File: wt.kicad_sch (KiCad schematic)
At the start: 20 parts, among them U1 STM32F407VGTx, Y1 Crystal_8Mhz

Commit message: working on AD inputs
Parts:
- removed C7: C-Pol-1uF-FK-V, Capacitor_SMD:C_1206_3216Metric, symbol eurorack:C-Pol-1uF-FK-V
- added C7: C-Pol-1uF-TAN, Capacitor_Tantalum_SMD:CP_EIA-3216-18_Kemet-A, symbol eurorack:C-Pol-1uF-TAN
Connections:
- net +3V3: now also C7.1
- net GND: now also C7.2

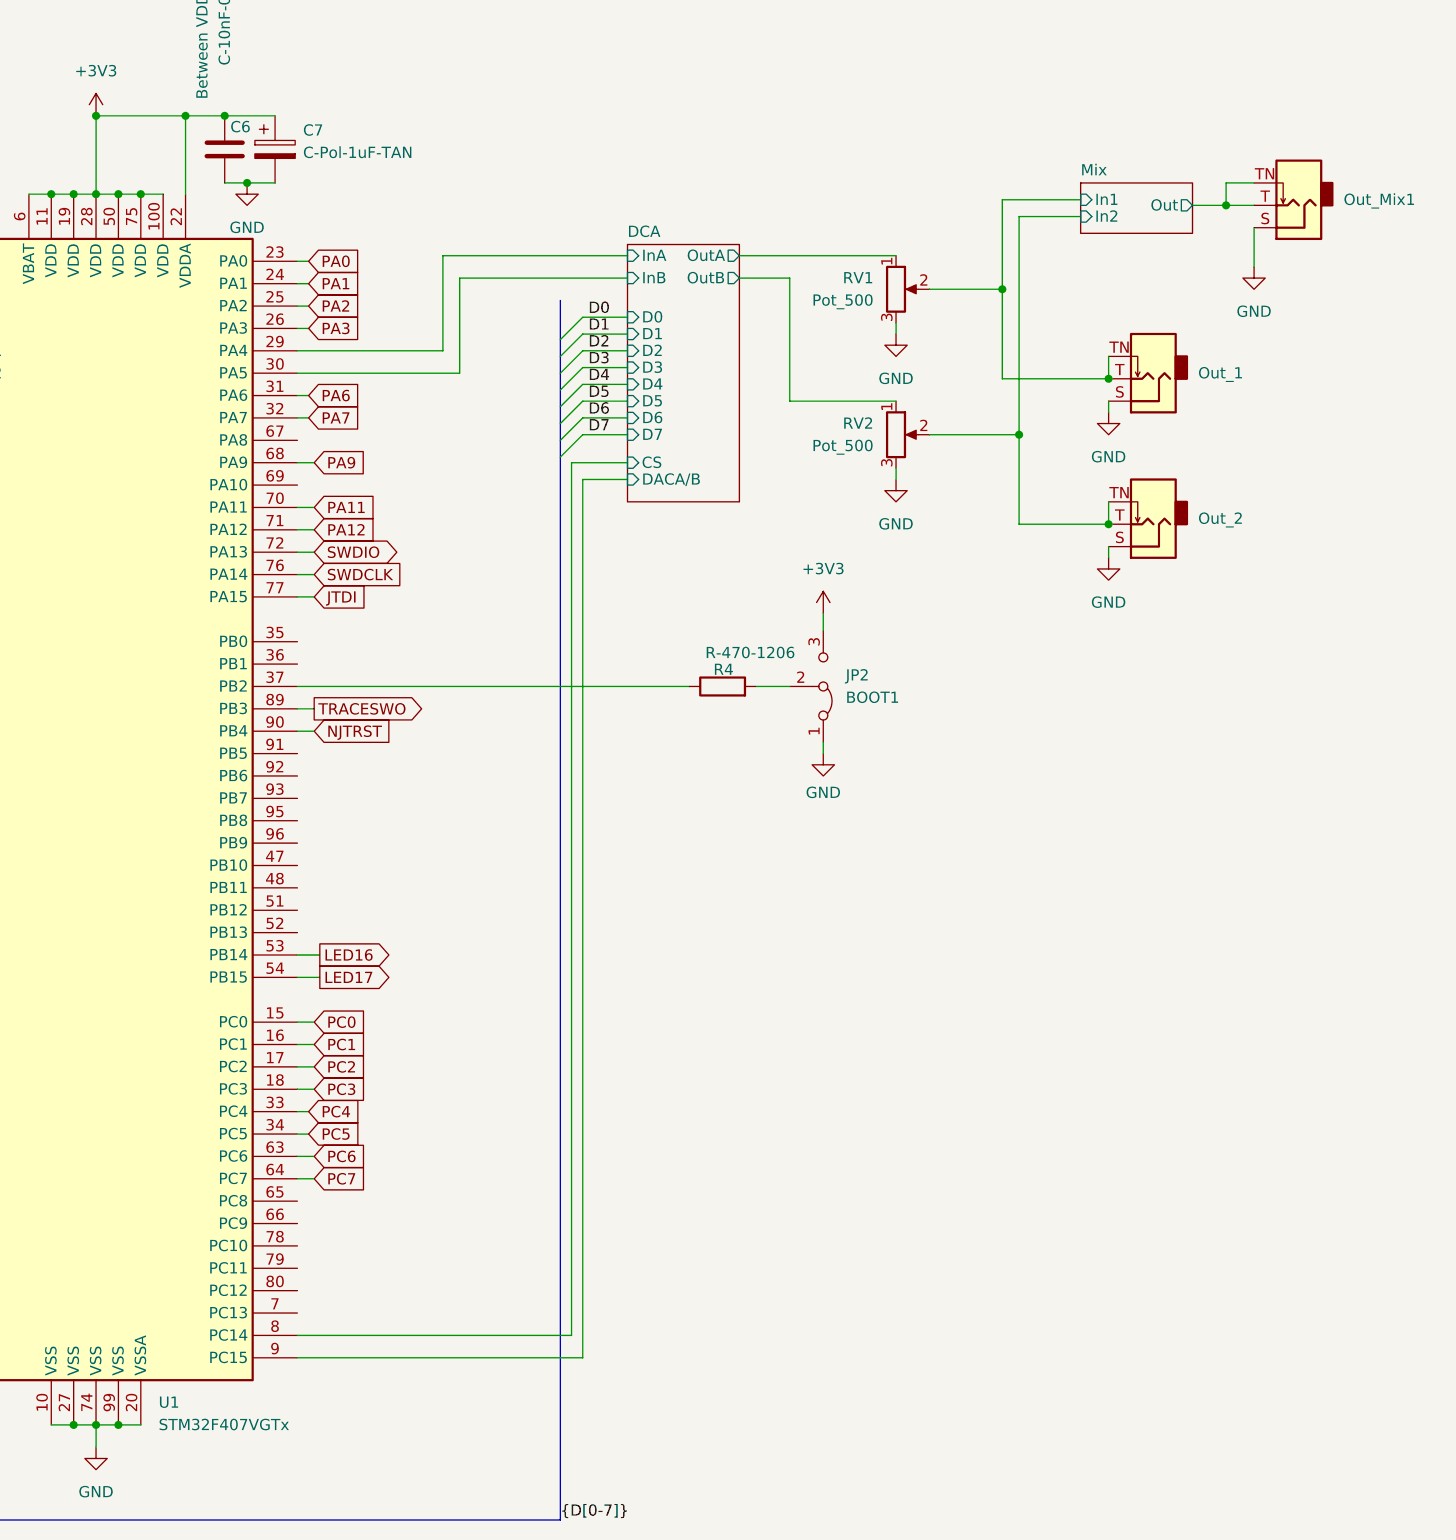
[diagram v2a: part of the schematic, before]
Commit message: reannotated changed to LM324
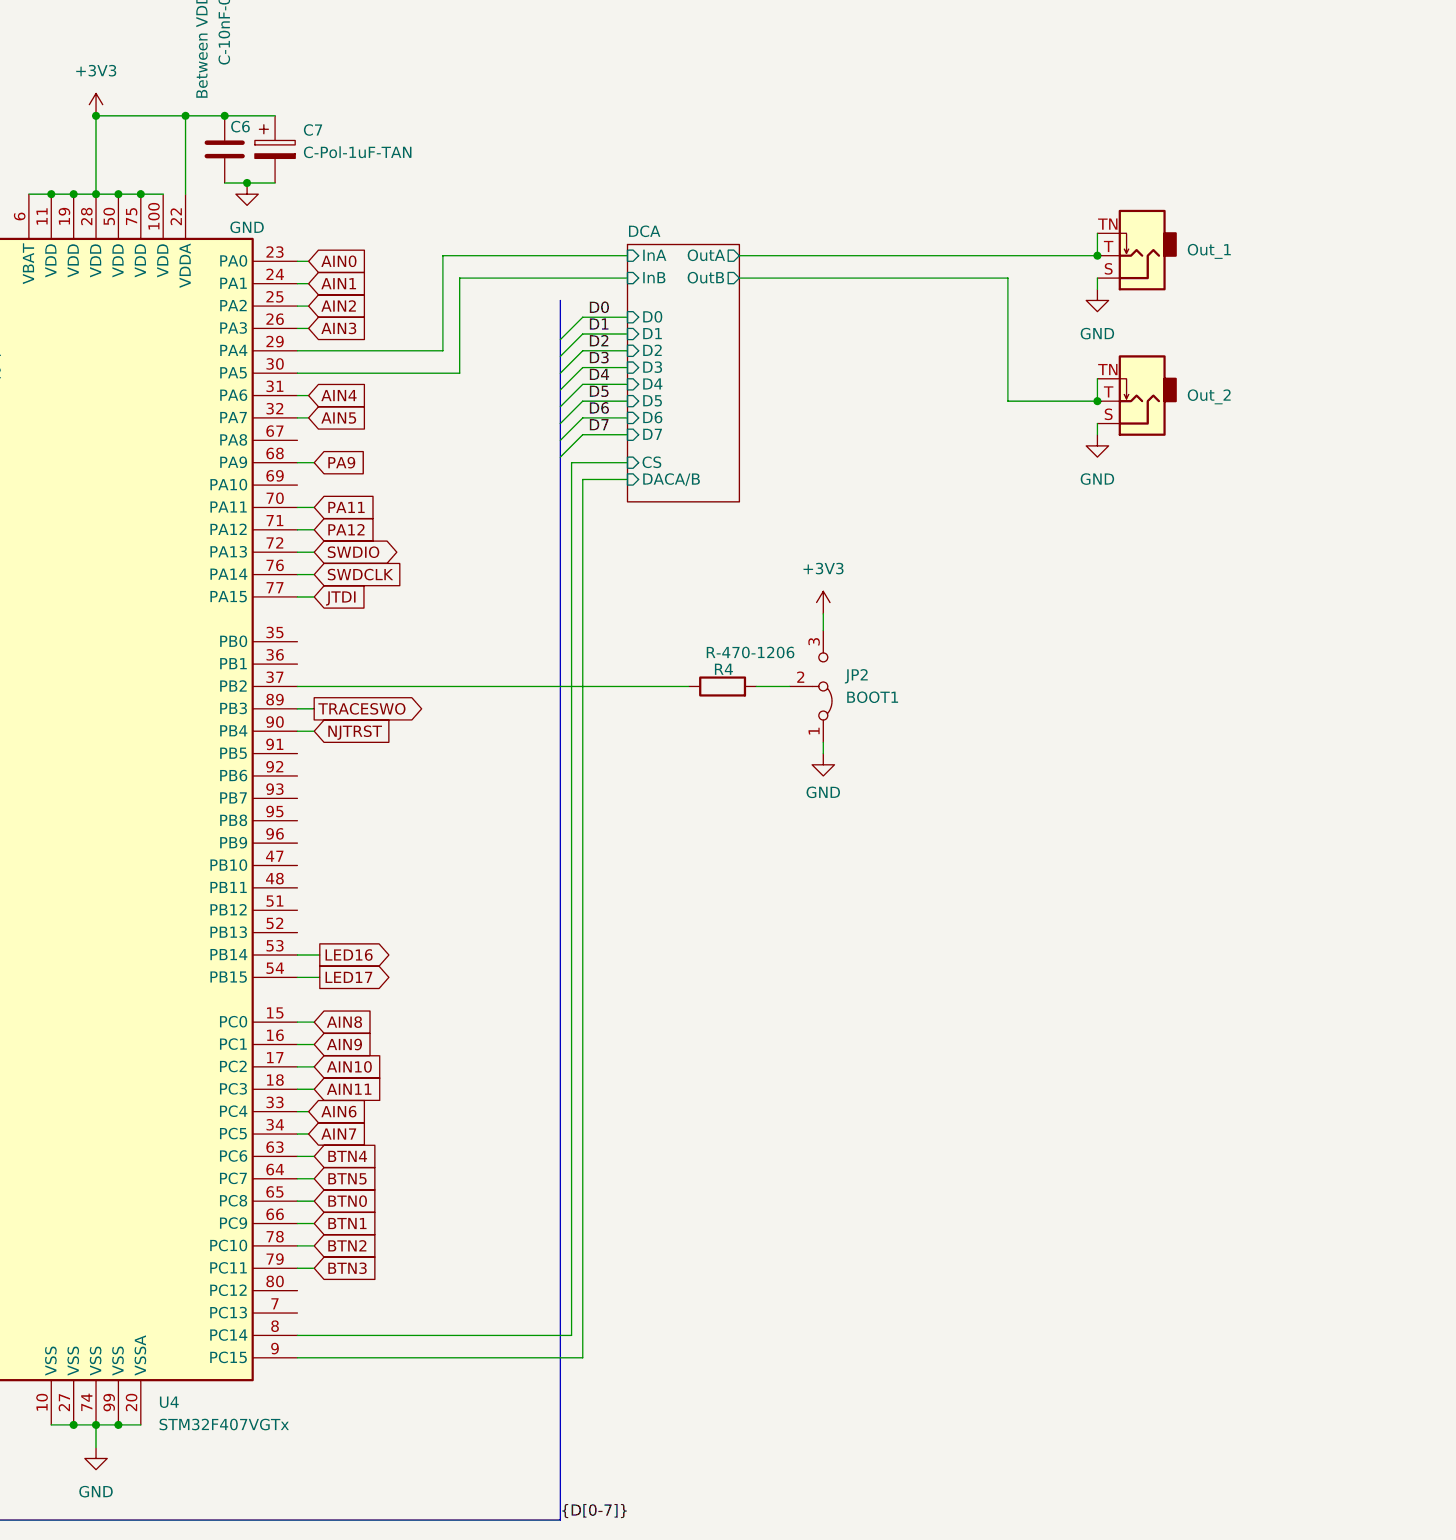
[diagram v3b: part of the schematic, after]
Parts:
- removed Out_Mix1: LUM-1502-03_3.5mm_mono_vertical_jack, eurorack:LUM 1502-03, symbol eurorack:LUM-1502-03_3.5mm_mono_vertical_jack
- removed RV1, RV2: Pot_500, Potentiometer_THT:Potentiometer_Piher_PT-10-V10_Vertical, symbol eurorack:Pot_500
- renumbered U1 to U4
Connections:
- net Mix/In1 is gone; now on net DCA/OutA: Out_1.T, Out_1.TN
- net Mix/In2 is gone; now on net DCA/OutB: Out_2.T, Out_2.TN
- net BTN0: now reaches U4.65 (PC8)
- net BTN1: now reaches U4.66 (PC9)
- net BTN2: now reaches U4.78 (PC10)
- net BTN3: now reaches U4.79 (PC11)
- net PA0 renamed AIN0
- net PA1 renamed AIN1
- net PA2 renamed AIN2
- net PA3 renamed AIN3
- net PA6 renamed AIN4
- net PA7 renamed AIN5
- net PC0 renamed AIN8
- net PC1 renamed AIN9
- net PC2 renamed AIN10
- net PC3 renamed AIN11
- net PC4 renamed AIN6
- net PC5 renamed AIN7
- net PC6 renamed BTN4
- net PC7 renamed BTN5
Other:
- removed sheet Mix
- moved on the sheet: Out_1, Out_2

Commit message: working on PCB, new iteratrion
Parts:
- JP1, JP2: footprint Connector_PinSocket_2.54mm:PinSocket_1x03_P2.54mm_Vertical -> Jumper:SolderJumper-3_P1.3mm_Open_RoundedPad1.0x1.5mm
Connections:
- net PA11 renamed USB_D-
- net PA12 renamed USB_D+
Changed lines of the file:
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@@
     )
   )
-  (global_label "PA12" (shape input) (at 210.82 125.73 0) (fields_autoplaced)
-    (effects (font (size 1.27 1.27)) (justify left))
-    (property "Intersheet References" "${INTERSHEET_REFS}" (id 0) (at 218.0107 125.6506 0)
+  (global_label "USB_D+" (shape input) (at 210.82 125.73 0) (fields_autoplaced)
+    (effects (font (size 1.27 1.27)) (justify left))
+    (property "Intersheet References" "${INTERSHEET_REFS}" (id 0) (at 220.8531 125.6506 0)
       (effects (font (size 1.27 1.27)) (justify left) hide)
     )
@@
     )
   )
-  (global_label "PA11" (shape input) (at 210.82 123.19 0) (fields_autoplaced)
-    (effects (font (size 1.27 1.27)) (justify left))
-    (property "Intersheet References" "${INTERSHEET_REFS}" (id 0) (at 218.0107 123.1106 0)
+  (global_label "USB_D-" (shape input) (at 210.82 123.19 0) (fields_autoplaced)
+    (effects (font (size 1.27 1.27)) (justify left))
+    (property "Intersheet References" "${INTERSHEET_REFS}" (id 0) (at 220.8531 123.1106 0)
       (effects (font (size 1.27 1.27)) (justify left) hide)
     )
@@
       (effects (font (size 1.27 1.27)) (justify left))
     )
-    (property "Footprint" "Connector_PinSocket_2.54mm:PinSocket_1x03_P2.54mm_Vertical" (id 2) (at 112.395 100.33 0)
+    (property "Footprint" "Jumper:SolderJumper-3_P1.3mm_Open_RoundedPad1.0x1.5mm" (id 2) (at 112.395 100.33 0)
       (effects (font (size 1.27 1.27)) hide)
     )
@@
       (effects (font (size 1.27 1.27)) (justify left))
     )
-    (property "Footprint" "Connector_PinSocket_2.54mm:PinSocket_1x03_P2.54mm_Vertical" (id 2) (at 268.605 143.51 0)
+    (property "Footprint" "Jumper:SolderJumper-3_P1.3mm_Open_RoundedPad1.0x1.5mm" (id 2) (at 268.605 143.51 0)
       (effects (font (size 1.27 1.27)) hide)
     )
@@
     )
     (path "/55f62779-ad1a-4899-b894-15cdd1ec3e8e"
-      (reference "JP1") (unit 1) (value "BOOT0") (footprint "Connector_PinSocket_2.54mm:PinSocket_1x03_P2.54mm_Vertical")
+      (reference "JP1") (unit 1) (value "BOOT0") (footprint "Jumper:SolderJumper-3_P1.3mm_Open_RoundedPad1.0x1.5mm")
     )
     (path "/7950cf24-2f5b-405d-8f12-5c081d409735"
-      (reference "JP2") (unit 1) (value "BOOT1") (footprint "Connector_PinSocket_2.54mm:PinSocket_1x03_P2.54mm_Vertical")
+      (reference "JP2") (unit 1) (value "BOOT1") (footprint "Jumper:SolderJumper-3_P1.3mm_Open_RoundedPad1.0x1.5mm")
     )
     (path "/c5361e3e-2aef-494b-b75e-964fb5c67e4f"

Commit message: working on the PCB
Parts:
- C4, C5: footprint Capacitor_SMD:C_1812_4532Metric_Pad1.57x3.40mm_HandSolder -> Capacitor_SMD:C_0603_1608Metric; symbol eurorack:C-2u2-1812 -> eurorack:C-2u2-0603
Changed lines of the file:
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@@
     (pin "2")
   )
-  (symbol (lib_id "eurorack:C-2u2-1812") (at 144.145 111.125 270) (unit 1)
+  (symbol (lib_id "eurorack:C-2u2-0603") (at 144.145 111.125 270) (unit 1)
     (in_bom yes) (on_board yes)
     (property "Reference" "C5" (id 0) (at 145.415 113.03 90)
@@
       (effects (font (size 1.27 1.27)) (justify left))
     )
-    (property "Footprint" "Capacitor_SMD:C_1812_4532Metric_Pad1.57x3.40mm_HandSolder" (id 2) (at 140.335 112.0902 0)
-      (effects (font (size 1.27 1.27)) hide)
-    )
-    (property "Datasheet" "https://secure.reichelt.com/at/en/mlcc-1812-2-2-f-100-v-10--ecc-kts101b225k-p256478.html?search=2.2+uF&&r=1" (id 3) (at 144.145 111.125 0)
+    (property "Footprint" "Capacitor_SMD:C_0603_1608Metric" (id 2) (at 140.335 112.0902 0)
+      (effects (font (size 1.27 1.27)) hide)
+    )
+    (property "Datasheet" "https://www.reichelt.com/at/en/smd-multilayer-capacitor-g0603-2-2-f-10-v-x7r-g0603-2-2-10-p89723.html?&trstct=pos_5&nbc=1" (id 3) (at 144.145 111.125 0)
       (effects (font (size 1.27 1.27)) hide)
     )
@@
     (pin "2")
   )
-  (symbol (lib_id "eurorack:C-2u2-1812") (at 144.145 105.41 270) (unit 1)
+  (symbol (lib_id "eurorack:C-2u2-0603") (at 144.145 105.41 270) (unit 1)
     (in_bom yes) (on_board yes)
     (property "Reference" "C4" (id 0) (at 145.415 104.14 90)
@@
       (effects (font (size 1.27 1.27)) (justify left))
     )
-    (property "Footprint" "Capacitor_SMD:C_1812_4532Metric_Pad1.57x3.40mm_HandSolder" (id 2) (at 140.335 106.3752 0)
-      (effects (font (size 1.27 1.27)) hide)
-    )
-    (property "Datasheet" "https://secure.reichelt.com/at/en/mlcc-1812-2-2-f-100-v-10--ecc-kts101b225k-p256478.html?search=2.2+uF&&r=1" (id 3) (at 144.145 105.41 0)
+    (property "Footprint" "Capacitor_SMD:C_0603_1608Metric" (id 2) (at 140.335 106.3752 0)
+      (effects (font (size 1.27 1.27)) hide)
+    )
+    (property "Datasheet" "https://www.reichelt.com/at/en/smd-multilayer-capacitor-g0603-2-2-f-10-v-x7r-g0603-2-2-10-p89723.html?&trstct=pos_5&nbc=1" (id 3) (at 144.145 105.41 0)
       (effects (font (size 1.27 1.27)) hide)
     )
@@
     )
     (path "/60bc7c03-463a-43e6-8f17-71fb7806a209"
-      (reference "C4") (unit 1) (value "C-2u2-1812") (footprint "Capacitor_SMD:C_1812_4532Metric_Pad1.57x3.40mm_HandSolder")
+      (reference "C4") (unit 1) (value "C-2u2-1812") (footprint "Capacitor_SMD:C_0603_1608Metric")
     )
     (path "/35225c69-6fe2-4a15-9fc8-d82d764c75e3"
-      (reference "C5") (unit 1) (value "C-2u2-1812") (footprint "Capacitor_SMD:C_1812_4532Metric_Pad1.57x3.40mm_HandSolder")
+      (reference "C5") (unit 1) (value "C-2u2-1812") (footprint "Capacitor_SMD:C_0603_1608Metric")
     )
     (path "/31959283-2eba-44a6-b213-87d4ded9f599"

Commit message: reworking with Pot Lights
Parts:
- removed JP2: BOOT1, Jumper:SolderJumper-3_P1.3mm_Open_RoundedPad1.0x1.5mm, symbol Jumper:Jumper_3_Bridged12
- JP1: footprint Jumper:SolderJumper-3_P1.3mm_Open_RoundedPad1.0x1.5mm -> Connector_PinHeader_2.54mm:PinHeader_1x03_P2.54mm_Vertical
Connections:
- net GND: now also R4.2
- net AIN0-LED: now reaches U4.35 (PB0)
- net AIN1-LED: now reaches U4.36 (PB1)
- net AIN7-LED: now reaches U4.47 (PB10)
- net AIN8-LED: now reaches U4.48 (PB11)
- net AIN9-LED: now reaches U4.51 (PB12)
- net AIN10-LED: now reaches U4.52 (PB13)
- net AIN11-LED: now reaches U4.69 (PA10)
- net AIN2-LED: now reaches U4.91 (PB5)
- net AIN3-LED: now reaches U4.92 (PB6)
- net AIN4-LED: now reaches U4.93 (PB7)
- net AIN5-LED: now reaches U4.95 (PB8)
- net AIN6-LED: now reaches U4.96 (PB9)
